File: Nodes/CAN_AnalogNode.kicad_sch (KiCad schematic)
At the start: 17 parts, among them IC4 TCAN1462VDRQ1, IC5 TCAN1462VDRQ1, SW1 CAS-220TB1

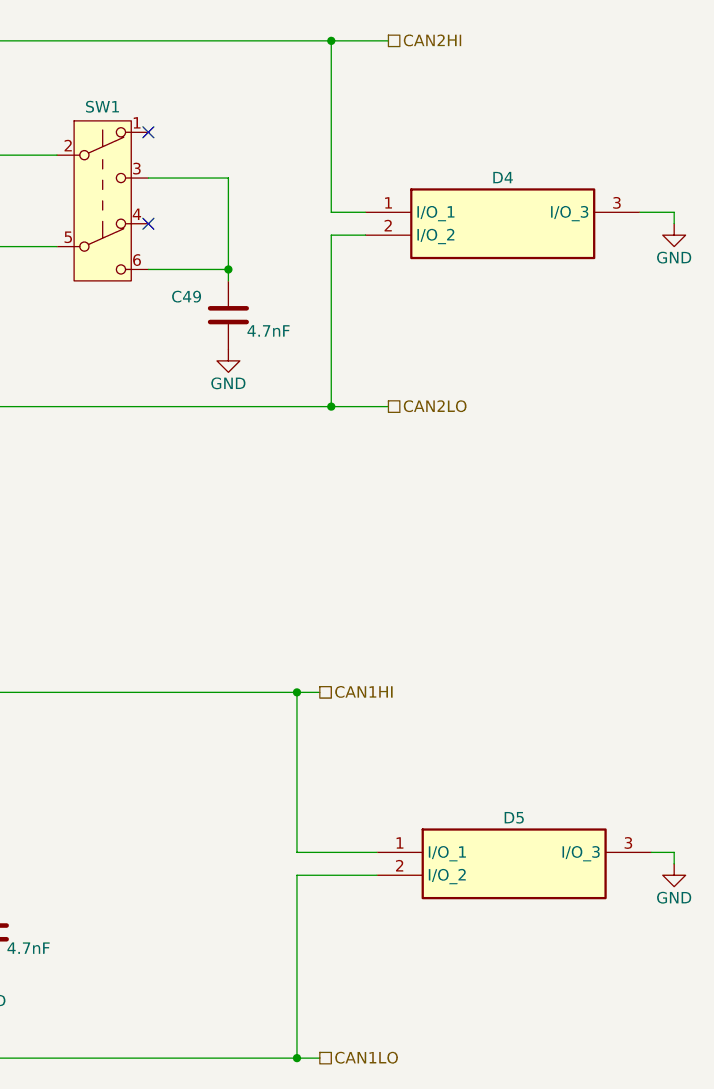
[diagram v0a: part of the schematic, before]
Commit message: Nodes v2.1.2 Improved
- Improved schematic design
- Added two 4.7 uF caps according to the datasheets of the microchips
- Other small changes
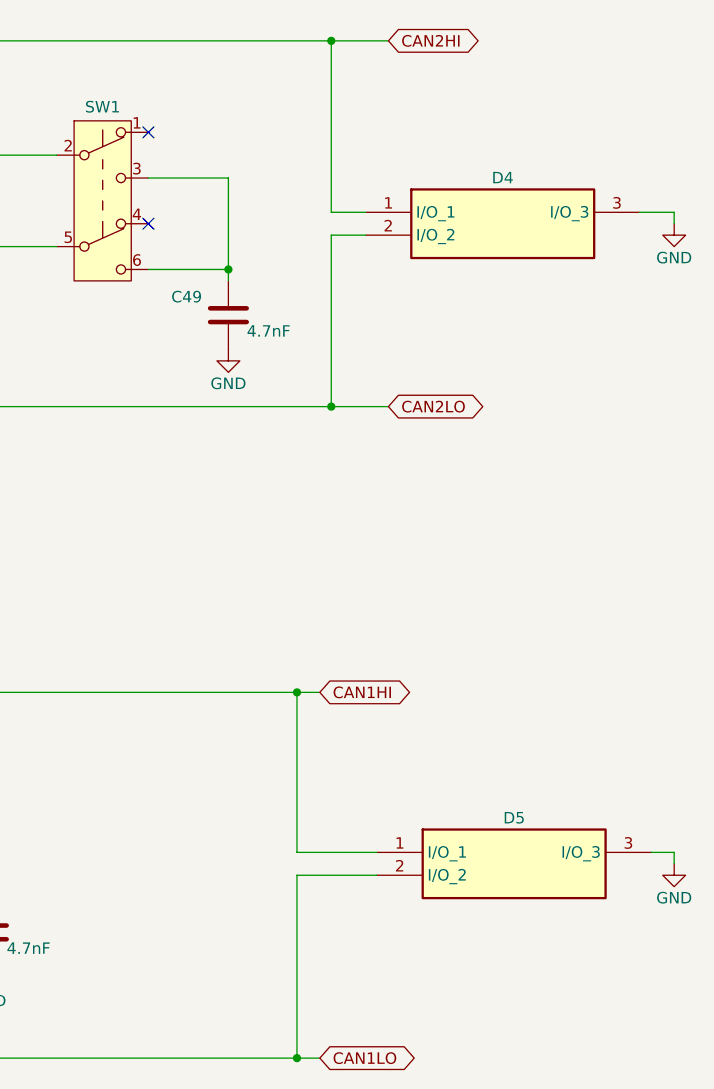
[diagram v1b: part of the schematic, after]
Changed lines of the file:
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@@
+		)
+	)
+	(global_label "CAN2LO"
+		(shape bidirectional)
+		(at 237.49 62.23 0)
+		(fields_autoplaced yes)
+		(effects
+			(font
+				(size 1.27 1.27)
+			)
+			(justify left)
+		)
+		(property "Intersheetrefs" "${INTERSHEET_REFS}"
+			(at 248.8437 62.23 0)
+			(effects
+				(font
+					(size 1.27 1.27)
+				)
+				(justify left)
+				(hide yes)
+			)
+		)
+	)
+	(global_label "CAN1LO"
+		(shape bidirectional)
+		(at 229.87 134.62 0)
+		(fields_autoplaced yes)
+		(effects
+			(font
+				(size 1.27 1.27)
+			)
+			(justify left)
+		)
+		(property "Intersheetrefs" "${INTERSHEET_REFS}"
+			(at 241.2237 134.62 0)
+			(effects
+				(font
+					(size 1.27 1.27)
+				)
+				(justify left)
+				(hide yes)
+			)
+		)
+	)
+	(global_label "CAN1HI"
+		(shape bidirectional)
+		(at 229.87 93.98 0)
+		(fields_autoplaced yes)
+		(effects
+			(font
+				(size 1.27 1.27)
+			)
+			(justify left)
+		)
+		(property "Intersheetrefs" "${INTERSHEET_REFS}"
+			(at 240.8004 93.98 0)
+			(effects
+				(font
+					(size 1.27 1.27)
+				)
+				(justify left)
+				(hide yes)
+			)
+		)
+	)
+	(global_label "CAN2HI"
+		(shape bidirectional)
+		(at 237.49 21.59 0)
+		(fields_autoplaced yes)
+		(effects
+			(font
+				(size 1.27 1.27)
+			)
+			(justify left)
+		)
+		(property "Intersheetrefs" "${INTERSHEET_REFS}"
+			(at 248.4204 21.59 0)
+			(effects
+				(font
+					(size 1.27 1.27)
+				)
+				(justify left)
+				(hide yes)
+			)
 		)
 	)
@@
 			)
 			(justify right)
-		)
-	)
-	(hierarchical_label "CAN1HI"
-		(shape passive)
-		(at 229.87 93.98 0)
-		(fields_autoplaced yes)
-		(effects
-			(font
-				(size 1.27 1.27)
-			)
-			(justify left)
-		)
-	)
-	(hierarchical_label "CAN2HI"
-		(shape passive)
-		(at 237.49 21.59 0)
-		(fields_autoplaced yes)
-		(effects
-			(font
-				(size 1.27 1.27)
-			)
-			(justify left)
-		)
-	)
-	(hierarchical_label "CAN1LO"
-		(shape passive)
-		(at 229.87 134.62 0)
-		(fields_autoplaced yes)
-		(effects
-			(font
-				(size 1.27 1.27)
-			)
-			(justify left)
 		)
 	)
@@
 		)
 	)
-	(hierarchical_label "CAN2LO"
-		(shape passive)
-		(at 237.49 62.23 0)
-		(fields_autoplaced yes)
-		(effects
-			(font
-				(size 1.27 1.27)
-			)
-			(justify left)
-		)
-	)

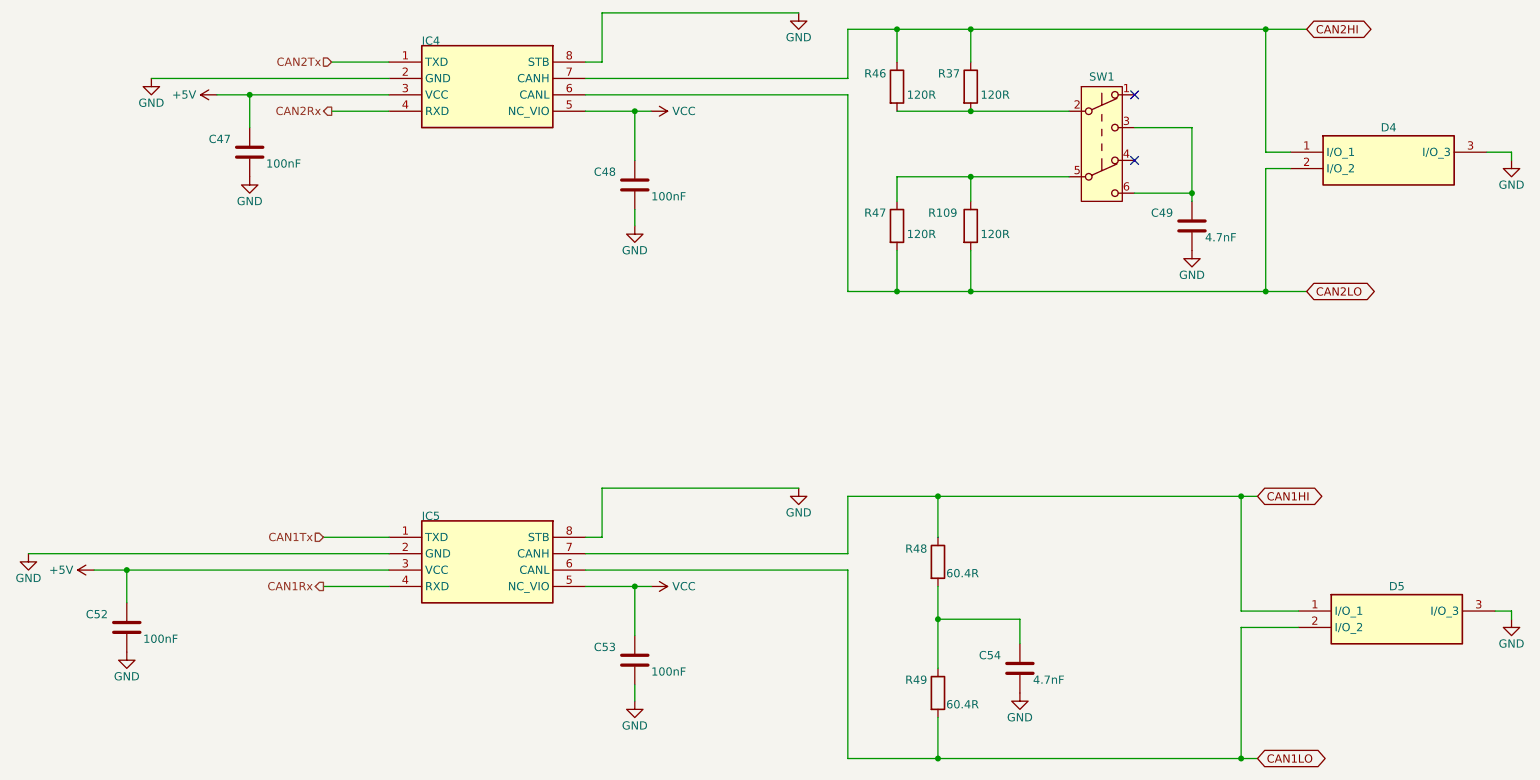
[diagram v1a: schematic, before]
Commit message: Nodes v2.2
- This version not compatible with BOB v.2.1.2 and older!
- Completely new layout design
- New power supply system with new voltage regulators
- New microchip STM32G431RBTx for the Analog Node
- New connection system (instead of 18 pin headers now 8 pin and pins were grouped by functions)
- Reduced size of the board by 5%
- Removed power switch for the Analog Node (because this functionality is now provided by a separate voltage regulator. for a more stable voltage)
- Removable ground from the holes added
- Layer numbers added
- Small improvements of the components information were made
- New oscillator for the Nodes
- Removed CAN1, so now only one CAN connection due to the capabilities of the new microchip
- Other small changes and fixes on the schematic and design
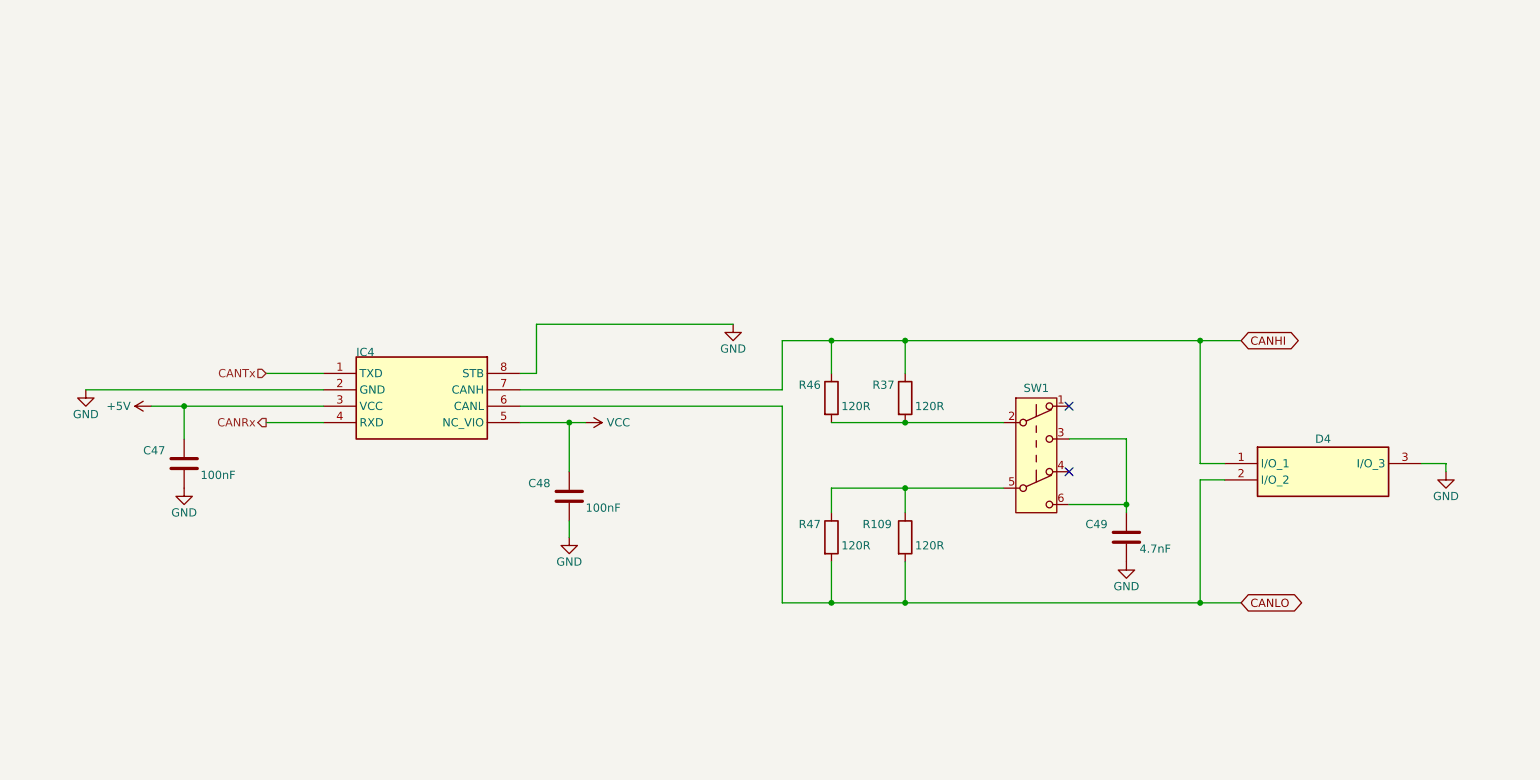
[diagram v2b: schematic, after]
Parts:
- removed C52, C53: 100nF, Capacitor_SMD:C_0805_2012Metric_Pad1.18x1.45mm_HandSolder, symbol Device:C
- removed C54: 4.7nF, Capacitor_SMD:C_0805_2012Metric_Pad1.18x1.45mm_HandSolder, symbol Device:C
- removed D5: ESDCAN24-2BLY, Diode_SMD:SOT95P255X125-3N, symbol ESDCAN24-2BLY:ESDCAN24-2BLY
- removed IC5: TCAN1462VDRQ1, SamacSys.PcbLib:SOIC127P600X175-8N, symbol Untitled-altium-import:root_0_TCAN1462VDRQ1
- removed R48, R49: 60.4R, Resistor_SMD:R_0805_2012Metric_Pad1.20x1.40mm_HandSolder, symbol Device:R
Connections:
- net CAN2HI renamed CANHI
- net CAN2LO renamed CANLO
- net CAN2Rx renamed CANRx
- net CAN2Tx renamed CANTx
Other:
- moved on the sheet: C47, C48, C49, D4, IC4, R109, R37, R46, R47, SW1

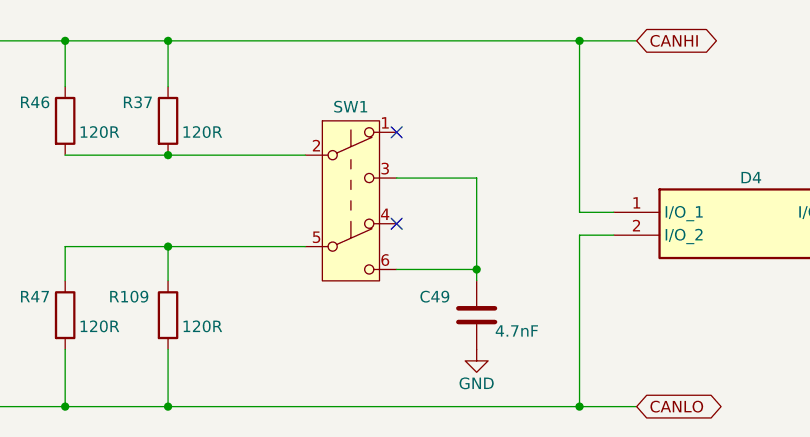
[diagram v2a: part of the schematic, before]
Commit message: Nodes v2.2.3
- Added one more PWM Level shifter
- Controllable amplitude of PWM by switches
- Added labels
- Added resistors to solve BOOT issue
- I2C1 pins changed
- More GND vias
- Higher resistance for adjustable voltage regulators
- Other small changes
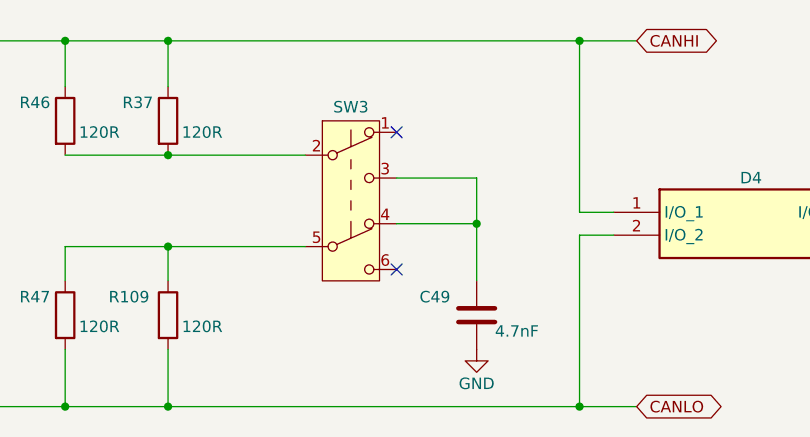
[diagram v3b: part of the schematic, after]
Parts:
- renumbered SW1 to SW3
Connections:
- net at C49.1, SW3.3 (C): now also SW3.4 (A); no longer SW3.6 (C)
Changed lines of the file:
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@@
+	)
+	(junction
+		(at 209.55 90.17)
+		(diameter 0)
+		(color 0 0 0 0)
 	)
 	(junction
@@
 		(color 0 0 0 0)
 	)
-	(junction
-		(at 209.55 95.25)
-		(diameter 0)
-		(color 0 0 0 0)
-	)
-	(no_connect
-		(at 200.66 90.17)
-	)
 	(no_connect
 		(at 200.66 80.01)
 	)
+	(no_connect
+		(at 200.66 95.25)
+	)
 	(wire
 		(pts
@@
 	(wire
 		(pts
-			(xy 200.66 95.25) (xy 209.55 95.25)
-		)
-		(stroke
-			(width 0)
-			(type default)
-		)
-	)
-	(wire
-		(pts
 			(xy 123.19 90.17) (xy 123.19 82.55)
 		)
@@
 	(wire
 		(pts
-			(xy 209.55 85.09) (xy 209.55 95.25)
+			(xy 209.55 85.09) (xy 209.55 90.17)
 		)
 		(stroke
@@
 	(wire
 		(pts
+			(xy 200.66 90.17) (xy 209.55 90.17)
+		)
+		(stroke
+			(width 0)
+			(type default)
+		)
+	)
+	(wire
+		(pts
 			(xy 163.83 92.71) (xy 163.83 96.52)
 		)
@@
 	(wire
 		(pts
+			(xy 209.55 90.17) (xy 209.55 96.52)
+		)
+		(stroke
+			(width 0)
+			(type default)
+		)
+	)
+	(wire
+		(pts
 			(xy 175.26 82.55) (xy 190.5 82.55)
 		)
@@
 		(pts
 			(xy 156.21 77.47) (xy 115.57 77.47)
-		)
-		(stroke
-			(width 0)
-			(type default)
-		)
-	)
-	(wire
-		(pts
-			(xy 209.55 95.25) (xy 209.55 96.52)
 		)
 		(stroke
@@
 		(on_board yes)
 		(dnp no)
-		(property "Reference" "SW1"
+		(property "Reference" "SW3"
 			(at 195.58 77.216 0)
 			(effects
@@
 			(project "Nodes"
 				(path "/7f1aa41b-970a-42cc-8701-1d90e3bd89a6/7d82bd19-4de3-497f-a840-7872f07b0c7c/77be9626-821e-42de-9f62-115b4450057f"
-					(reference "SW1")
+					(reference "SW3")
 					(unit 1)
 				)
